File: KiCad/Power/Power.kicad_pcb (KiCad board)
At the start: 2 copper layers, 97 x 98 mm, 49 parts, among them J1 Screw_Terminal_01x04, J2 Screw_Terminal_01x03, J3 Screw_Terminal_01x03, J4 Screw_Terminal_01x02, SW1 SW_DPST, U1 CD74HC4051E, U2 TL074, U3 L7805, U4 L7905

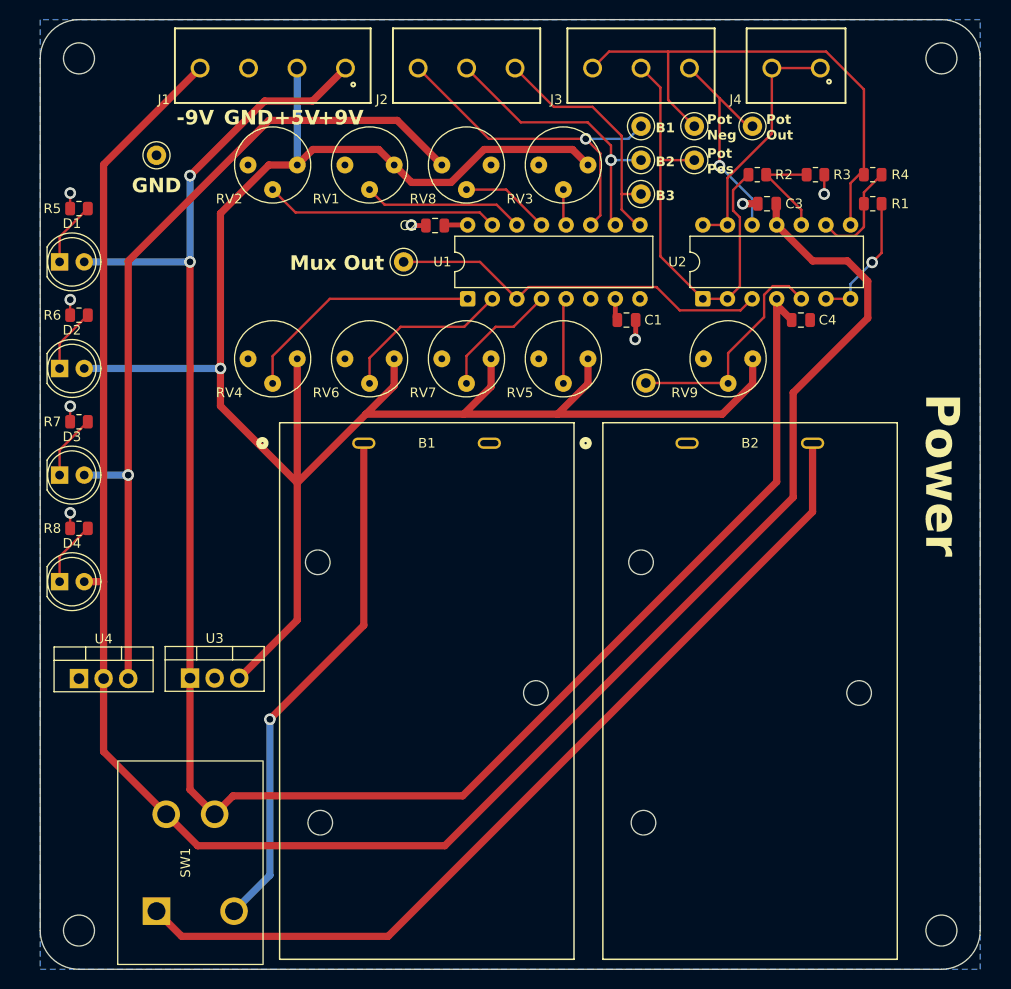
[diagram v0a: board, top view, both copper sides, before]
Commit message: updated power board to have more terminals
before, the power board had only one terminal for power supply, so the other boards would share this terminal. now, the power board has a terminal for each other board, so the other boards don't need to share the same terminal for power
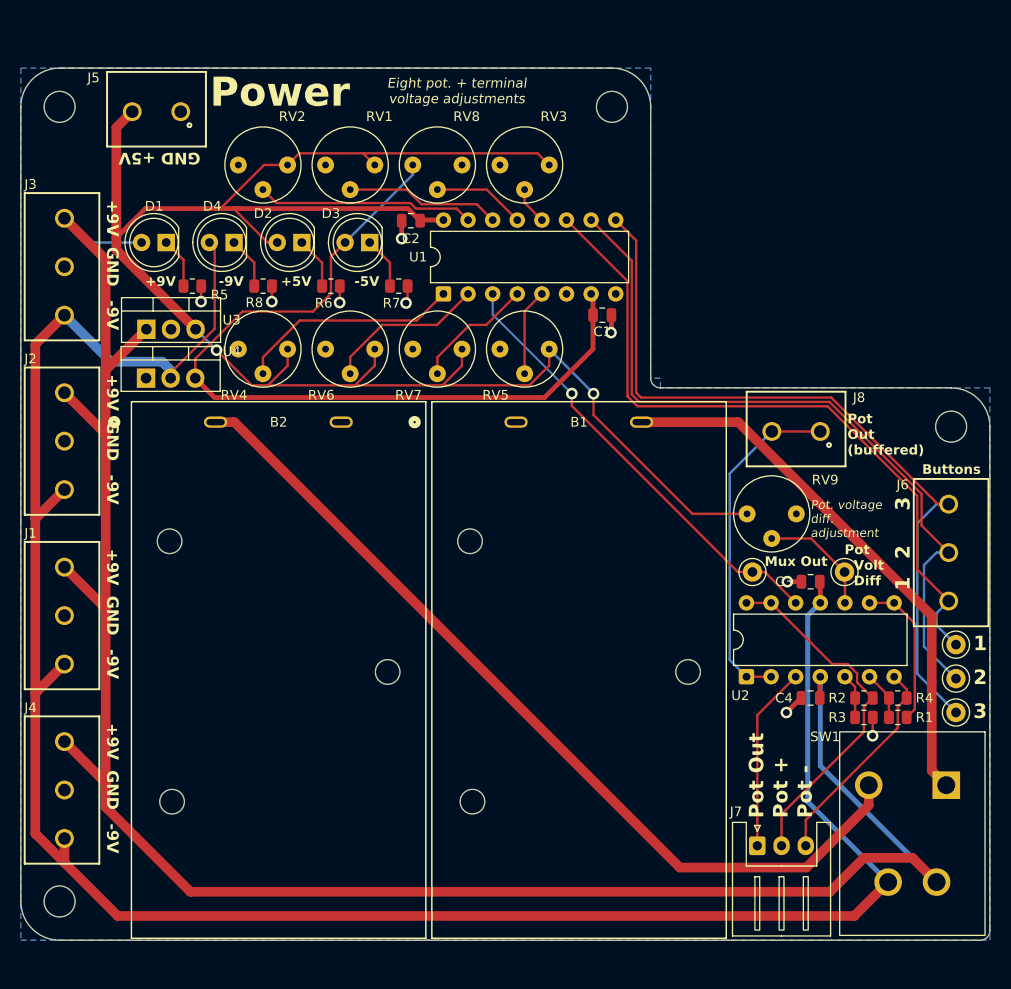
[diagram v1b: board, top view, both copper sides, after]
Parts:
- removed TP3, TP4, TP5, TP6: TestPoint_Small, TestPoint:TestPoint_Keystone_5000-5004_Miniature
- added J5: Screw_Terminal_01x02, Header 691137710002:691137710002, F.Cu at (31.0, 32.5)
- added J6: Screw_Terminal_01x03, Header 691137710003:691137710003, F.Cu at (112.8, 78.0)
- added J7: Conn_01x03, Connector_JST:JST_XH_S3B-XH-A_1x03_P2.50mm_Horizontal, F.Cu at (93.0, 108.2)
- added J8: Screw_Terminal_01x02, Header 691137710002:691137710002, F.Cu at (97.0, 65.5)
- J1: value Screw_Terminal_01x04 -> Screw_Terminal_01x03; footprint Header 691137710004:691137710004 -> Header 691137710003:691137710003
- J4: value Screw_Terminal_01x02 -> Screw_Terminal_01x03; footprint Header 691137710002:691137710002 -> Header 691137710003:691137710003
- moved J4 106.1 mm to (21.5, 102.5), turned to -90 degrees
- moved H3 91.5 mm to (78.0, 32.0)
- moved SW1 74.6 mm to (109.0, 107.0), turned to -90 degrees
- moved J3 62.9 mm to (21.5, 48.5), turned to -90 degrees
- moved TP11 62.6 mm to (113.5, 87.5)
- moved TP12 62.6 mm to (113.5, 91.0)
- moved TP13 62.6 mm to (113.5, 94.5)
- moved J1 60.5 mm to (21.5, 84.5), turned to -90 degrees
- moved J2 56.6 mm to (21.5, 66.5), turned to -90 degrees
- moved R3 56.2 mm to (104.0, 95.0)
- moved R2 55.1 mm to (104.0, 93.0), turned to 180 degrees
- moved R4 54.1 mm to (107.5, 93.0), turned to 0 degrees
- moved R1 53.1 mm to (107.5, 95.0)
- moved B2 48.7 mm to (37.1, 64.5)
- moved TP1 48.2 mm to (92.5, 80.0)
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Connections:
- B1 pad 1: Net-(B1-Pad1) -> GND
- B1 pad 2: GND -> Net-(B1-Pad2)
- B2 pad 1: GND -> Net-(B2-Pad1)
- B2 pad 2: Net-(B2-Pad2) -> GND
- J1 pad 2: +5V -> GND
- J1 pad 3: GND -> -9V
- J2 pad 1: /Button 3 -> +9V
- J2 pad 2: /Button 2 -> GND
- J2 pad 3: /Button 1 -> -9V
- J3 pad 1: /Pot Out -> +9V
- J3 pad 2: /Pot + -> GND
- J3 pad 3: /Pot - -> -9V
- J4 pad 1: /Buffered Pot Out -> +9V
- J4 pad 2: /Buffered Pot Out -> GND
- R1 pad 1: Net-(U2B--) -> Net-(U2C--)
- R1 pad 2: Net-(U2C--) -> Net-(U2B--)
- R2 pad 2: Net-(U2C-+) -> Net-(U2B-+)
- R3 pad 2: Net-(U2C-+) -> Net-(U2B-+)
- R4 pad 1: Net-(U2C--) -> Net-(U2B--)
- RV9 pad 1: +5V -> GND
- RV9 pad 3: GND -> +5V
- SW1 pad 1: Net-(B2-Pad2) -> Net-(B1-Pad2)
- SW1 pad 2: -9V -> +9V
- SW1 pad 3: Net-(B1-Pad1) -> Net-(B2-Pad1)
- SW1 pad 4: +9V -> -9V
- U2 pad 1: /Pot + -> /Buffered Pot Out
- U2 pad 10: Net-(U2C-+) -> /Pot Voltage Difference
- U2 pad 12: /Pot Out -> /Mux Out
- U2 pad 13: /Buffered Pot Out -> /Pot +
- U2 pad 14: /Buffered Pot Out -> /Pot +
- U2 pad 2: /Pot + -> /Buffered Pot Out
- U2 pad 3: /Mux Out -> /Pot Out
- U2 pad 5: /Pot Voltage Difference -> Net-(U2B-+)
- U2 pad 7: Net-(U2B--) -> /Pot -
- U2 pad 8: /Pot - -> Net-(U2C--)
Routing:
- net Net-(B2-Pad2): track 94.0 -> 0.00 mm
- net Net-(B2-Pad1): track 0.00 -> 91.2 mm
- net Net-(B1-Pad2): track 0.00 -> 56.3 mm
- net /Button 3: track 26.0 -> 80.9 mm
- net Net-(B1-Pad1): track 53.8 -> 0.00 mm, vias 1 -> 0
- net /Button 2: track 29.8 -> 77.3 mm, vias 1 -> 0
- net /Button 1: track 36.5 -> 73.0 mm, vias 1 -> 0
- net /Pot -: track 54.0 -> 22.3 mm
- net +9V: track 192.4 -> 215.7 mm, vias 2 -> 0
- net +5V: track 211.8 -> 190.9 mm, vias 1 -> 2
- net -9V: track 206.2 -> 223.8 mm
- net /Pot Voltage Difference: track 23.9 -> 12.1 mm
- net Net-(U2C-+): track 10.9 -> 0.00 mm
- net /Pot +: track 46.8 -> 36.8 mm
- net /Buffered Pot Out: track 25.6 -> 35.4 mm
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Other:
- board size 97 x 98 mm -> 100 x 90 mm
- board text added: "-5V"
- board text added: "1"
- board text added: "2"
- board text added: "3"
- board text added: "Buttons"
- board text added: "Eight pot. + terminal voltage adjustments"
- board text added: "Pot +"
- board text added: "Pot -"
- board text added: "Pot Out (buffered)"
- board text added: "Pot Volt Diff"
- board text added: "Pot. voltage diff. adjustment"
- board text removed: "B1"
- board text removed: "B2"
- board text removed: "B3"
- board text removed: "Pot Neg"
- board text removed: "Pot Pos"

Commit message: added silkscreen to help assembly process on all boards
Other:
- board text added: "+ LDO"
- board text added: "100k"
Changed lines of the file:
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@@
 		)
 		(property "Value" "TL074"
-			(at 3.81 17.57 90)
-			(layer "F.Fab")
+			(at 3.81 7.62 180)
+			(layer "F.SilkS")
 			(effects
 				(font
@@
 		(tags "TO-220-3 Vertical RM 2.54mm")
 		(property "Reference" "U3"
-			(at 8.79 -0.95 0)
+			(at -1.96 -3.95 0)
 			(layer "F.SilkS")
 			(effects
@@
 		(tags "TO-220-3 Vertical RM 2.54mm")
 		(property "Reference" "U4"
-			(at 8.83 -2.75 0)
+			(at -3.92 -2 0)
 			(layer "F.SilkS")
 			(effects
@@
 		)
 		(property "Value" "CD74HC4051E"
-			(at 3.81 20.11 90)
-			(layer "F.Fab")
+			(at 3.805 8.89 180)
+			(layer "F.SilkS")
 			(effects
 				(font
@@
 		)
 	)
+	(gr_text "+ LDO"
+		(at 30.5 52.5 0)
+		(layer "F.SilkS")
+		(effects
+			(font
+				(size 1 1)
+				(thickness 0.15)
+			)
+		)
+	)
+	(gr_text "100k"
+		(at 42 36 0)
+		(layer "F.SilkS")
+		(effects
+			(font
+				(size 1 1)
+				(thickness 0.15)
+			)
+		)
+	)
+	(gr_text "100k"
+		(at 42 55 0)
+		(layer "F.SilkS")
+		(effects
+			(font
+				(size 1 1)
+				(thickness 0.15)
+			)
+		)
+	)
+	(gr_text "100k"
+		(at 51 36 0)
+		(layer "F.SilkS")
+		(effects
+			(font
+				(size 1 1)
+				(thickness 0.15)
+			)
+		)
+	)
+	(gr_text "100k"
+		(at 51 55 0)
+		(layer "F.SilkS")
+		(effects
+			(font
+				(size 1 1)
+				(thickness 0.15)
+			)
+		)
+	)
+	(gr_text "100k"
+		(at 60 36 0)
+		(layer "F.SilkS")
+		(effects
+			(font
+				(size 1 1)
+				(thickness 0.15)
+			)
+		)
+	)
+	(gr_text "100k"
+		(at 60 55 0)
+		(layer "F.SilkS")
+		(effects
+			(font
+				(size 1 1)
+				(thickness 0.15)
+			)
+		)
+	)
+	(gr_text "100k"
+		(at 69 36 0)
+		(layer "F.SilkS")
+		(effects
+			(font
+				(size 1 1)
+				(thickness 0.15)
+			)
+		)
+	)
+	(gr_text "100k"
+		(at 69 55 0)
+		(layer "F.SilkS")
+		(effects
+			(font
+				(size 1 1)
+				(thickness 0.15)
+			)
+		)
+	)
+	(gr_text "100k"
+		(at 94.5 72 0)
+		(layer "F.SilkS")
+		(effects
+			(font
+				(size 1 1)
+				(thickness 0.15)
+			)
+		)
+	)

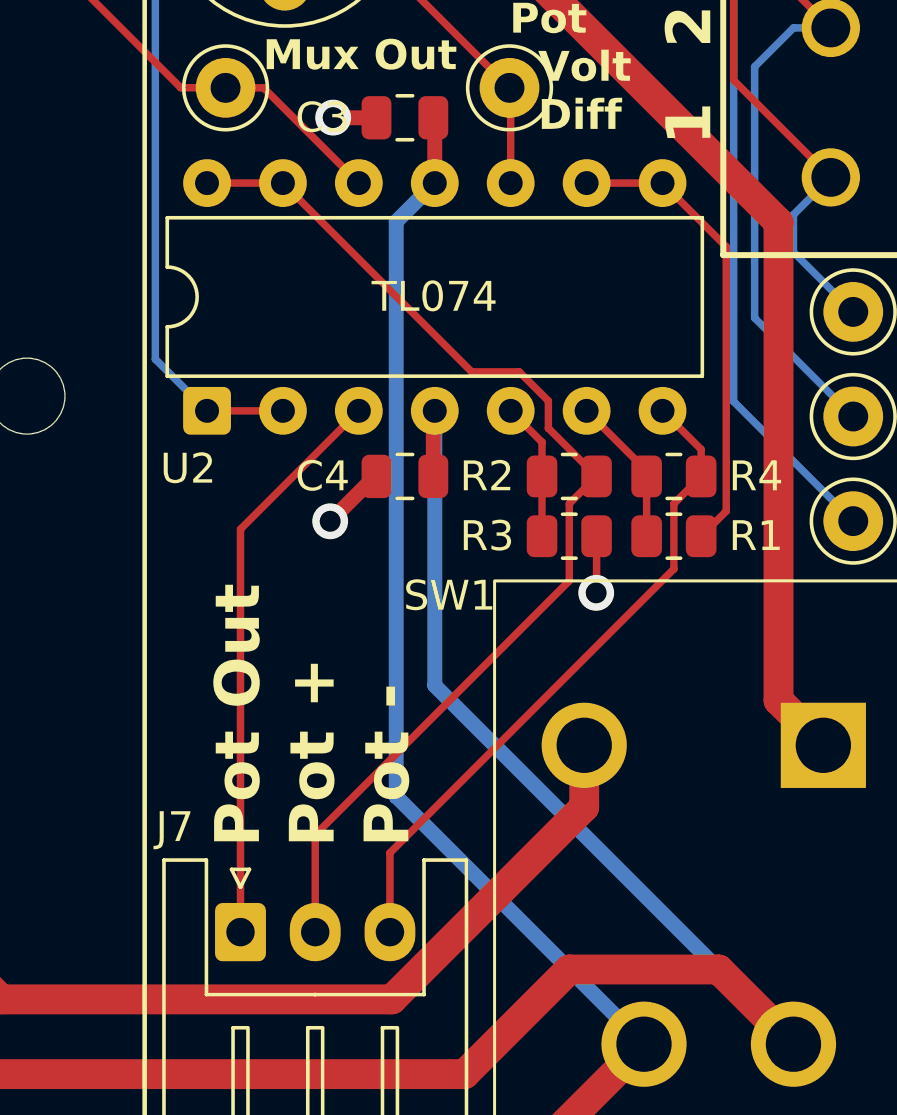
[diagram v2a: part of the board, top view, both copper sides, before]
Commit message: added protective resistor to op amp connecting to slide pot
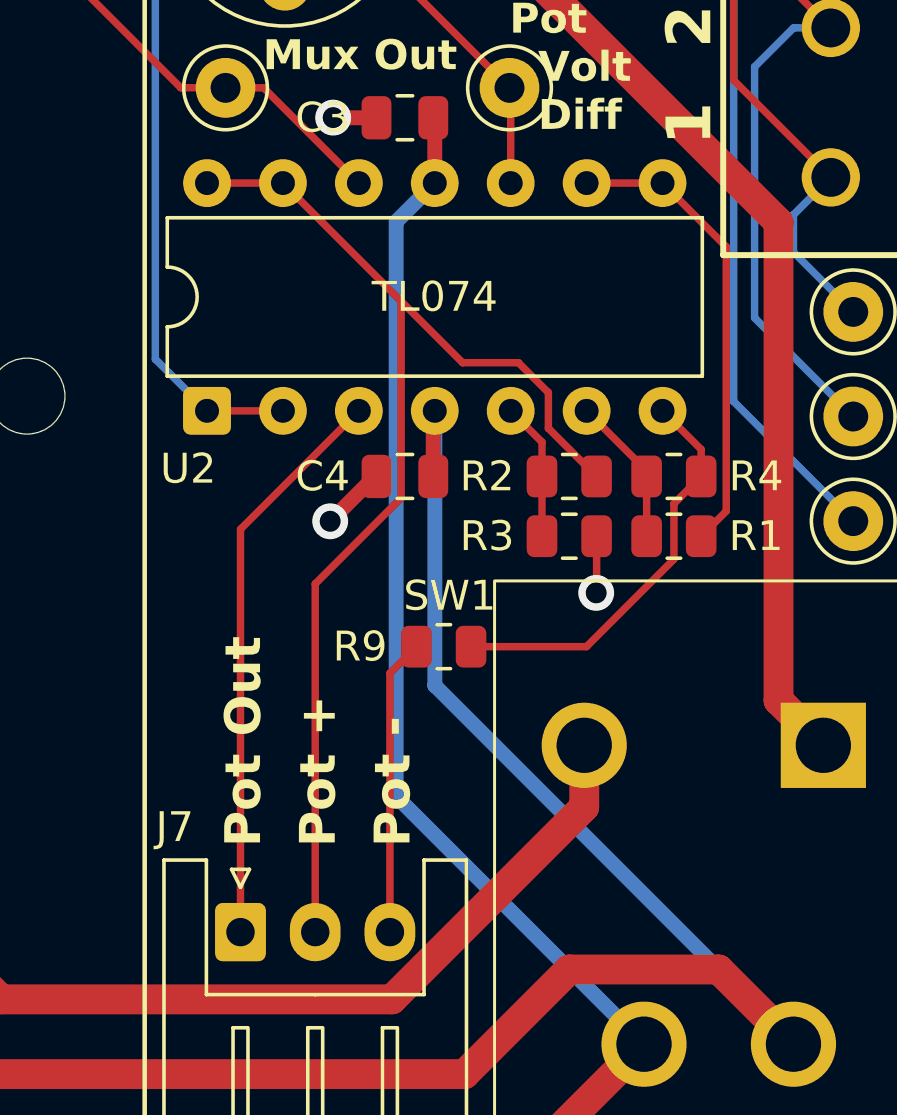
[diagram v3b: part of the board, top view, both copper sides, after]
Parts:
- added R9: 2.2k, Resistor_SMD:R_0805_2012Metric, F.Cu at (99.8, 98.7)
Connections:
- R4 pad 2: /Pot - -> Net-(R4-Pad2)
- U2 pad 7: /Pot - -> Net-(R4-Pad2)
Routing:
- net Net-(R4-Pad2): track 0.00 -> 13.9 mm
- net /Pot -: track 22.3 -> 10.0 mm
- net /Pot +: track 36.8 -> 40.1 mm
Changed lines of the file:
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@@
 		)
 	)
+	(footprint "Resistor_SMD:R_0805_2012Metric"
+		(layer "F.Cu")
+		(at 99.8 98.7 180)
+		(descr "Resistor SMD 0805 (2012 Metric), square (rectangular) end terminal, IPC-7351 nominal, (Body size source: IPC-SM-782 page 72, https://www.pcb-3d.com/wordpress/wp-content/uploads/ipc-sm-782a_amendment_1_and_2.pdf)")
+		(tags "resistor")
+		(property "Reference" "R9"
+			(at 2.8 0 0)
+			(layer "F.SilkS")
+			(effects
+				(font
+					(size 1 1)
+					(thickness 0.15)
+				)
+			)
+		)
+		(property "Value" "2.2k"
+			(at 0 1.65 0)
+			(layer "F.Fab")
+			(effects
+				(font
+					(size 1 1)
+					(thickness 0.15)
+				)
+			)
+		)
+		(property "Datasheet" ""
+			(at 0 0 0)
+			(layer "F.Fab")
+			(hide yes)
+			(effects
+				(font
+					(size 1.27 1.27)
+				)
+			)
+		)
+		(property "Description" "Resistor, US symbol"
+			(at 0 0 0)
+			(layer "F.Fab")
+			(hide yes)
+			(effects
+				(font
+					(size 1.27 1.27)
+				)
+			)
+		)
+		(property "KiLib_Generator" "SMD_2terminal_chip_molded"
+			(at 0 0 0)
+			(layer "F.SilkS")
+			(hide yes)
+			(effects
+				(font
+					(size 1 1)
+					(thickness 0.15)
+				)
+			)
+		)
+		(property ki_fp_filters "R_*")
+		(sheetname "/")
+		(sheetfile "Power.kicad_sch")
+		(units
+			(unit
+				(name "A")
+				(pins "1" "2")
+			)
+		)
+		(attr smd)
+		(duplicate_pad_numbers_are_jumpers no)
+		(fp_line
+			(start -0.227064 0.735)
+			(end 0.227064 0.735)
+			(stroke
+				(width 0.12)
+				(type solid)
+			)
+			(layer "F.SilkS")
+		)
+		(fp_line
+			(start -0.227064 -0.735)
+			(end 0.227064 -0.735)
+			(stroke
+				(width 0.12)
+				(type solid)
+			)
+			(layer "F.SilkS")
+		)
+		(fp_rect
+			(start -1.68 -0.95)
+			(end 1.68 0.95)
+			(stroke
+				(width 0.05)
+				(type solid)
+			)
+			(fill no)
+			(layer "F.CrtYd")
+		)
+		(fp_rect
+			(start -1 -0.625)
+			(end 1 0.625)
+			(stroke
+				(width 0.1)
+				(type solid)
+			)
+			(fill no)
+			(layer "F.Fab")
+		)
+		(fp_text user "${REFERENCE}"
+			(at 0 0 0)
+			(layer "F.Fab")
+			(effects
+				(font
+					(size 0.5 0.5)
+					(thickness 0.08)
+				)
+			)
+		)
+		(pad "1" smd roundrect
+			(at -0.9125 0 180)
+			(size 1.025 1.4)
+			(layers "F.Cu" "F.Mask" "F.Paste")
+			(roundrect_rratio 0.243902)
+			(net "Net-(R4-Pad2)")
+			(pintype "passive")
+		)
+		(pad "2" smd roundrect
+			(at 0.9125 0 180)
+			(size 1.025 1.4)
+			(layers "F.Cu" "F.Mask" "F.Paste")
+			(roundrect_rratio 0.243902)
+			(net "/Pot -")
+			(pintype "passive")
+		)
+		(embedded_fonts no)
+		(model "${KICAD10_3DMODEL_DIR}/Resistor_SMD.3dshapes/R_0805_2012Metric.step"
+			(offset
+				(xyz 0 0 0)
+			)
+			(scale
+				(xyz 1 1 1)
+			)
+			(rotate
+				(xyz 0 0 0)
+			)
+		)
+	)
 	(footprint "Potentiometer_THT:Potentiometer_Bourns_3339P_Vertical_HandSoldering"
 		(layer "F.Cu")
@@
 			(layers "*.Cu" "*.Mask")
 			(remove_unused_layers no)
-			(net "/Pot -")
+			(net "Net-(R4-Pad2)")
 			(pintype "output")
 		)
@@
 			(layers "F.Cu" "F.Mask" "F.Paste")
 			(roundrect_rratio 0.243902)
-			(net "/Pot -")
+			(net "Net-(R4-Pad2)")
 			(pintype "passive")
 		)
@@
 		)
 	)
+	(gr_text "Pot Out"
+		(at 93.8 105.4 90)
+		(layer "F.SilkS")
+		(effects
+			(font
+				(size 1.2 1.2)
+				(thickness 0.24)
+				(bold yes)
+			)
+			(justify left bottom)
+		)
+	)
+	(gr_text "Pot +"
+		(at 96.3 105.4 90)
+		(layer "F.SilkS")
+		(effects
+			(font
+				(size 1.2 1.2)
+				(thickness 0.24)
+				(bold yes)
+			)
+			(justify left bottom)
+		)
+	)
+	(gr_text "Pot -"
+		(at 98.8 105.4 90)
+		(layer "F.SilkS")
+		(effects
+			(font
+				(size 1.2 1.2)
+				(thickness 0.24)
+				(bold yes)
+			)
+			(justify left bottom)
+		)
+	)
 	(gr_text "+5V"
 		(at 29 36.6 180)
@@
 		)
 	)
-	(gr_text "Pot Out"
-		(at 93.8 105.4 90)
-		(layer "F.SilkS")
-		(effects
-			(font
-				(size 1.5 1.5)
-				(thickness 0.3)
-				(bold yes)
-			)
-			(justify left bottom)
-		)
-	)
-	(gr_text "Pot +"
-		(at 96.3 105.4 90)
-		(layer "F.SilkS")
-		(effects
-			(font
-				(size 1.5 1.5)
-				(thickness 0.3)
-				(bold yes)
-			)
-			(justify left bottom)
-		)
-	)
-	(gr_text "Pot -"
-		(at 98.8 105.4 90)
-		(layer "F.SilkS")
-		(effects
-			(font
-				(size 1.5 1.5)
-				(thickness 0.3)
-				(bold yes)
-			)
-			(justify left bottom)
-		)
-	)
 	(gr_text "3"
 		(at 108.9 72.95 90)
@@
 	)
 	(segment
-		(start 108.4125 92.1025)
-		(end 107.12 90.81)
-		(width 0.25)
-		(layer "F.Cu")
-		(net "/Pot -")
-	)
-	(segment
-		(start 107.5 96.1)
-		(end 98 105.6)
+		(start 98.6875 99.1)
+		(end 98.7875 99.1)
 		(width 0.25)
 		(layer "F.Cu")
@@
 	)
 	(segment
-		(start 98 105.6)
-		(end 98 108.25)
+		(start 98 99.5875)
+		(end 98.8875 98.7)
 		(width 0.25)
 		(layer "F.Cu")
@@
 	)
 	(segment
-		(start 107.5 93.9175)
-		(end 107.5 96.1)
-		(width 0.25)
-		(layer "F.Cu")
-		(net "/Pot -")
-	)
-	(segment
-		(start 108.4125 93.005)
-		(end 108.4125 92.1025)
-		(width 0.25)
-		(layer "F.Cu")
-		(net "/Pot -")
-	)
-	(segment
-		(start 108.4125 93.005)
-		(end 107.5 93.9175)
+		(start 98 108.25)
+		(end 98 99.5875)
 		(width 0.25)
 		(layer "F.Cu")
@@
 	)
 	(segment
-		(start 103.3 90.479009)
-		(end 102.325991 89.505)
+		(start 103.3 90.2)
+		(end 102.3 89.2)
 		(width 0.25)
 		(layer "F.Cu")
@@
 	)
 	(segment
-		(start 100.735 89.505)
-		(end 94.42 83.19)
+		(start 100.43 89.2)
+		(end 98.375 87.145)
 		(width 0.25)
 		(layer "F.Cu")
@@
 	)
 	(segment
-		(start 104.9125 93.005)
-		(end 103.3 91.3925)
+		(start 95.5 96.6001)
+		(end 98.375 93.7251)
 		(width 0.25)
 		(layer "F.Cu")
@@
 	)
 	(segment
-		(start 104 93.9175)
-		(end 104 96.496852)
+		(start 95.5 108.25)
+		(end 95.5 96.6001)
 		(width 0.25)
 		(layer "F.Cu")
@@
 	)
 	(segment
-		(start 94.42 83.19)
-		(end 91.88 83.19)
+		(start 104.9125 93.005)
+		(end 103.3 91.3925)
 		(width 0.25)
 		(layer "F.Cu")
@@
 	)
 	(segment
-		(start 104 96.496852)
-		(end 95.5 104.996852)
+		(start 98.375 87.145)
+		(end 94.42 83.19)
 		(width 0.25)
 		(layer "F.Cu")
@@
 	)
 	(segment
-		(start 102.325991 89.505)
-		(end 100.735 89.505)
+		(start 98.375 93.7251)
+		(end 98.375 87.145)
 		(width 0.25)
 		(layer "F.Cu")
@@
 	)
 	(segment
-		(start 95.5 104.996852)
-		(end 95.5 108.25)
+		(start 102.3 89.2)
+		(end 100.43 89.2)
 		(width 0.25)
 		(layer "F.Cu")
@@
 	)
 	(segment
-		(start 104.9125 93.005)
-		(end 104 93.9175)
+		(start 94.42 83.19)
+		(end 91.88 83.19)
 		(width 0.25)
 		(layer "F.Cu")
@@
 	(segment
 		(start 103.3 91.3925)
-		(end 103.3 90.479009)
+		(end 103.3 90.2)
 		(width 0.25)
 		(layer "F.Cu")
@@
 		(net "/Pot+ 4th Partial")
 	)
+	(segment
+		(start 108.4125 92.1025)
+		(end 107.12 90.81)
+		(width 0.25)
+		(layer "F.Cu")
+		(net "Net-(R4-Pad2)")
+	)
+	(segment
+		(start 104.5751 98.7)
+		(end 107.5 95.7751)
+		(width 0.25)
+		(layer "F.Cu")
+		(net "Net-(R4-Pad2)")
+	)
+	(segment
+		(start 108.4125 93.005)
+		(end 108.4125 92.1025)
+		(width 0.25)
+		(layer "F.Cu")
+		(net "Net-(R4-Pad2)")
+	)
+	(segment
+		(start 100.7125 98.7)
+		(end 104.5751 98.7)
+		(width 0.25)
+		(layer "F.Cu")
+		(net "Net-(R4-Pad2)")
+	)
+	(segment
+		(start 107.5 93.9175)
+		(end 108.4125 93.005)
+		(width 0.25)
+		(layer "F.Cu")
+		(net "Net-(R4-Pad2)")
+	)
+	(segment
+		(start 107.5 95.7751)
+		(end 107.5 93.9175)
+		(width 0.25)
+		(layer "F.Cu")
+		(net "Net-(R4-Pad2)")
+	)
 	(zone
